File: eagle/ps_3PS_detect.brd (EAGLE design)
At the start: 122.9 x 120.3 mm, 16 parts, among them J1 PIN2F061.100, J2 PIN2F061.100

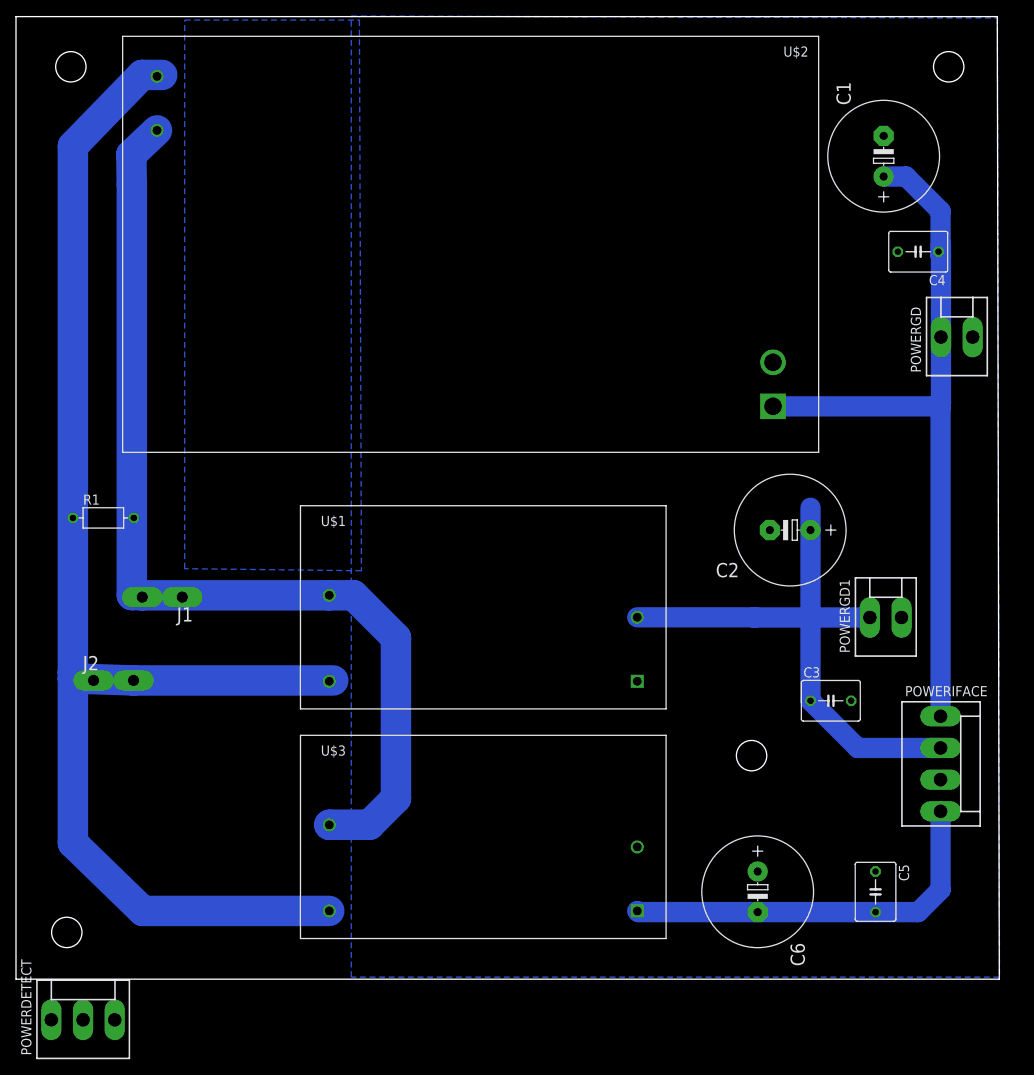
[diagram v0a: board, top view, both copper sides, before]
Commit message: update for thermal issues and CTIA breakout
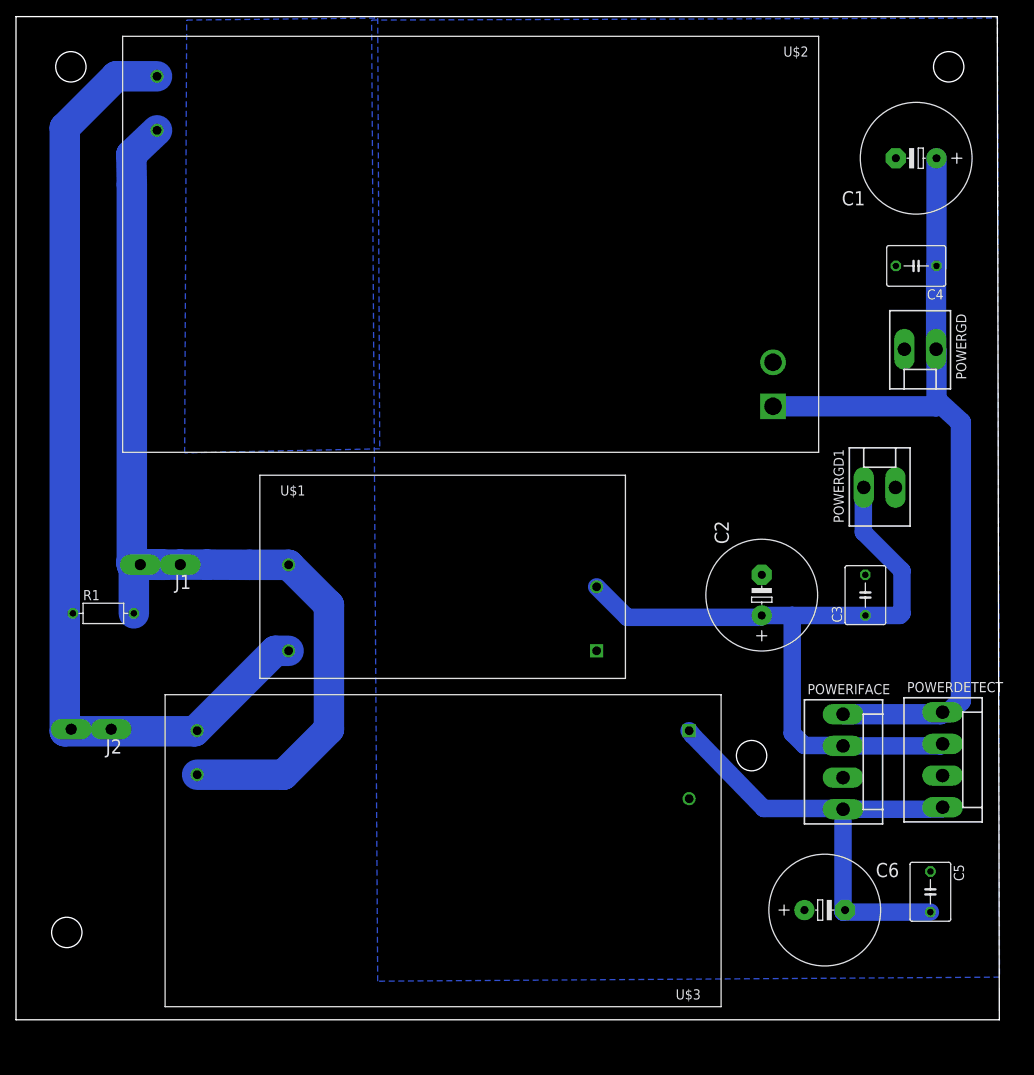
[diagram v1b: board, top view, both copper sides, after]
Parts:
- POWERDETECT: device con-molex:KK-156-3 -> con-molex:KK-156-4
- U$3: value IRM-05-05 -> IRM-30-15; device meanwell:IRM-05-05 -> meanwell:IRM-30-15
- moved POWERDETECT 112.3 mm to (115.3, 1.02), turned to 270 degrees
- moved U$3 60.8 mm to (87.6, 9.14), turned to 180 degrees
- moved POWERGD1 16.3 mm to (107.4, 35.1)
- moved C3 13.9 mm to (105.7, 21.6), turned to 90 degrees
- moved POWERIFACE 12.2 mm to (102.9, 0.76)
- moved R1 11.9 mm to (10.4, 19.3)
- moved C2 8.87 mm to (92.7, 21.6), turned to 90 degrees
- moved C6 8.69 mm to (100.6, -17.8), turned to 0 degrees
- moved C5 6.86 mm to (113.8, -15.5)
- moved J2 6.71 mm to (8.89, 4.83), turned to 180 degrees
- moved U$1 6.35 mm to (30.0, 11.2)
- moved POWERGD 4.82 mm to (112.5, 52.3), turned to 180 degrees
- moved J1 4.07 mm to (17.5, 25.4)
- moved C1 4.07 mm to (112.0, 76.2), turned to 180 degrees
- moved C4 1.80 mm to (112.0, 62.7)
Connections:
- removed net +12V: C1.+, C4.1, POWERGD.1, POWERIFACE.1, U$2.P$1
- removed net -5V: C5.2, C6.-, POWERDETECT.1, POWERIFACE.4, U$3.-V
- new net +15V: C1.+, C4.1, POWERDETECT.1, POWERGD.1, POWERIFACE.1, U$2.P$1
- new net -15V: C5.2, C6.-, POWERDETECT.4, POWERIFACE.4, U$3.-V
- net GND: now also POWERDETECT.3; no longer POWERDETECT.2
- net VCC: now also POWERDETECT.2; no longer POWERDETECT.3
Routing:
- net +15V: track 0.00 -> 105.8 mm
- net +12V: track 95.4 -> 0.00 mm
- net -15V: track 0.00 -> 60.5 mm
- net N$2: track 171.0 -> 121.8 mm
- net -5V: track 48.9 -> 0.00 mm
- net VCC: track 72.4 -> 92.0 mm
- net N$1: track 124.5 -> 127.5 mm
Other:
- board size 122.9 x 120.3 mm -> 122.9 x 125.4 mm
